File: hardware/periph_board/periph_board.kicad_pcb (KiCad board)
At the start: 2 copper layers, 149.7 x 25 mm, 49 parts, among them IC100 CD74HC4067SM96, IC101 LP2950-33LPRE3, IC102 ADC121S021CIMFX_NOPB, J100 2x10 Male Pins, U200 AH49HNTR-G1, U201 AH49HNTR-G1, U202 AH49HNTR-G1, U203 AH49HNTR-G1, U204 AH49HNTR-G1, U205 AH49HNTR-G1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

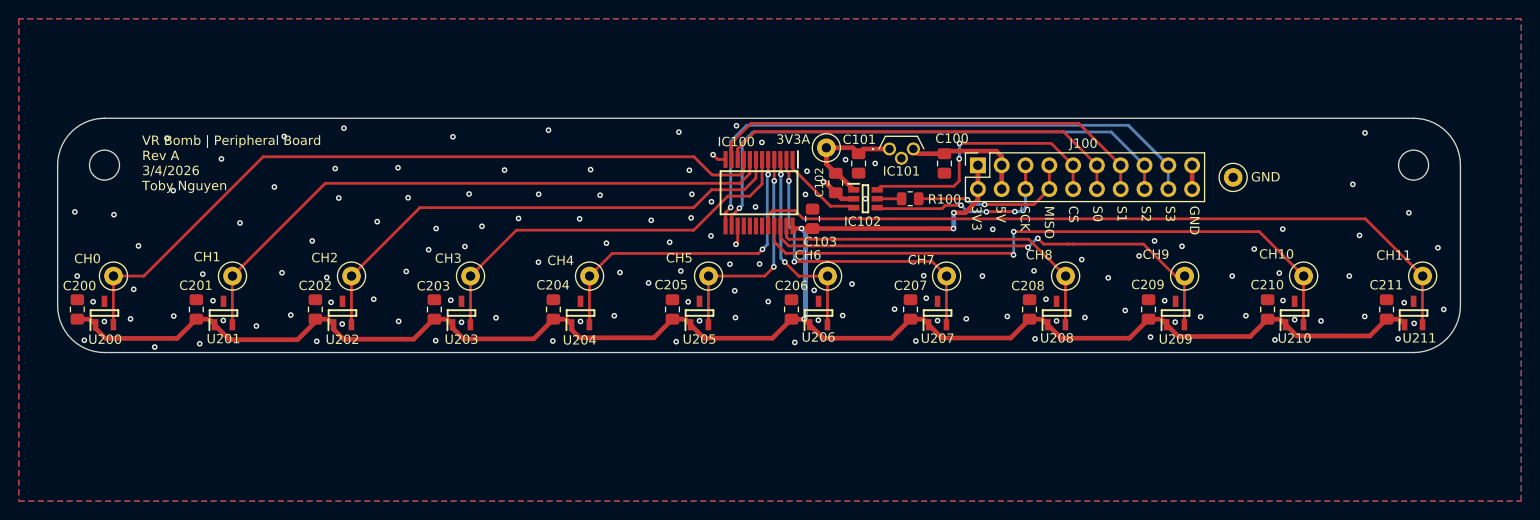
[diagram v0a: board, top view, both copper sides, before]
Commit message: replaced LDO thing to be free one in lab checkout. added some stuff to main board (wip)
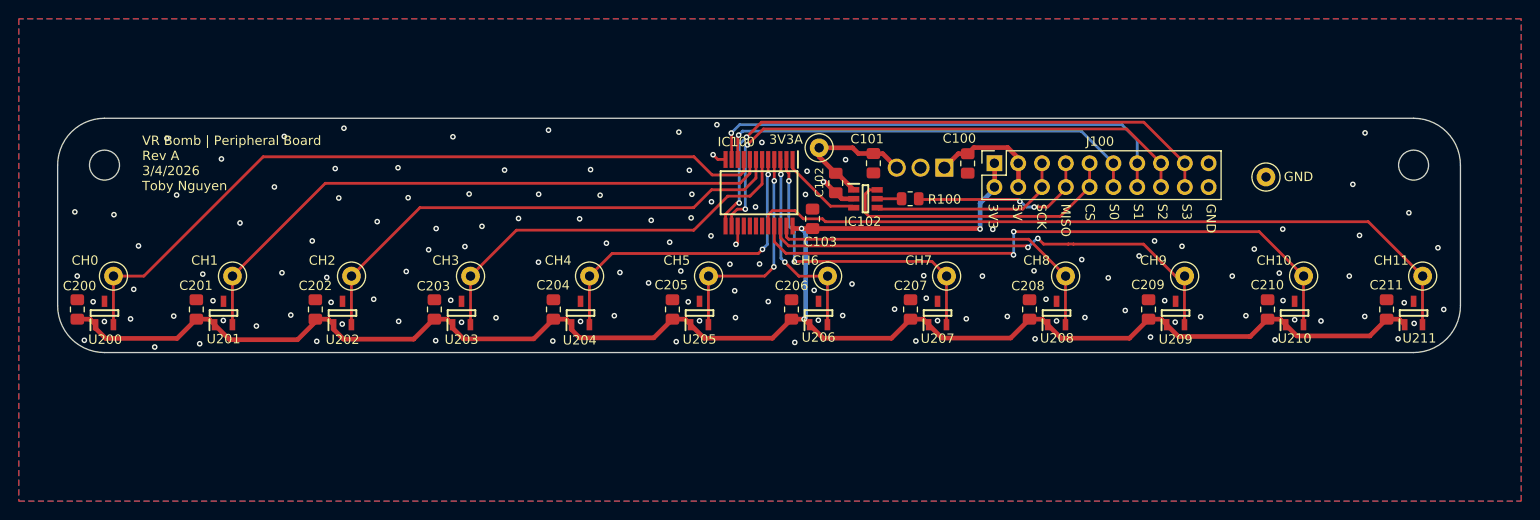
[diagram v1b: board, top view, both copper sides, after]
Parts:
- IC101: value LP2950-33LPRE3 -> LM2937ET-3.3_NOPB; footprint 445L:TL431CLPM -> 445L:TO254P470X1028X1955-3P; moved to B.Cu
- moved IC101 6.18 mm to (171.0, 79.9), turned to 180 degrees
- moved TP110 3.50 mm to (205.3, 80.9)
- moved C100 2.48 mm to (173.5, 79.4)
- moved J100 1.77 mm to (176.3, 79.4)
- moved C101 1.58 mm to (163.4, 79.4)
- moved TP103 0.77 mm to (157.7, 77.8)
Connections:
- IC101 pad 1: +3.3VADC -> +5V
- IC101 pad 3: +5V -> +3.3VADC
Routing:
- net /S1: track 48.6 -> 52.2 mm, vias 0 -> 1
- net /CS: track 28.8 -> 31.4 mm, vias 2 -> 0
- net GND: track 10.1 -> 7.56 mm, vias 139 -> 137
- net /S0: track 44.3 -> 46.8 mm, vias 0 -> 1
- net +3.3VADC: track 13.0 -> 15.3 mm
- net /MISO: track 17.4 -> 19.4 mm
- net /S2: track 56.8 -> 58.8 mm, vias 1 -> 2
- net +3V3: track 197.0 -> 198.8 mm, vias 4 -> 3
- net /S3: track 61.0 -> 62.3 mm, vias 1 -> 2
- net +5V: track 13.5 -> 12.5 mm
- net /SCK: track 21.0 -> 21.2 mm, vias 3 -> 0
